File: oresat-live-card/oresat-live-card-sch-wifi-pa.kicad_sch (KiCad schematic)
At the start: 29 parts, among them J9 U.FL, U17 PAT1220-C-3DB, U19 TQP9111, U8 MIC94070YC6-TR

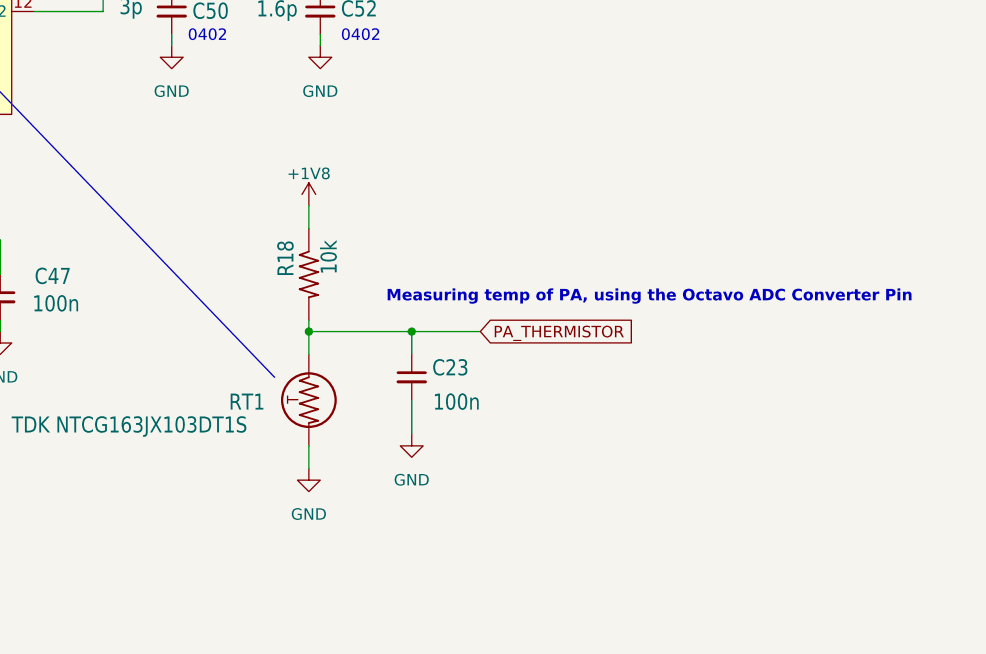
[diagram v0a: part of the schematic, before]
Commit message: Updated SIP A, B, and C. Lots of cleanup of crazy routing - this board is long in the tooth and has been rerouted several times, so there's a lot of crazy routing. Cleaning up a bit is really helping.
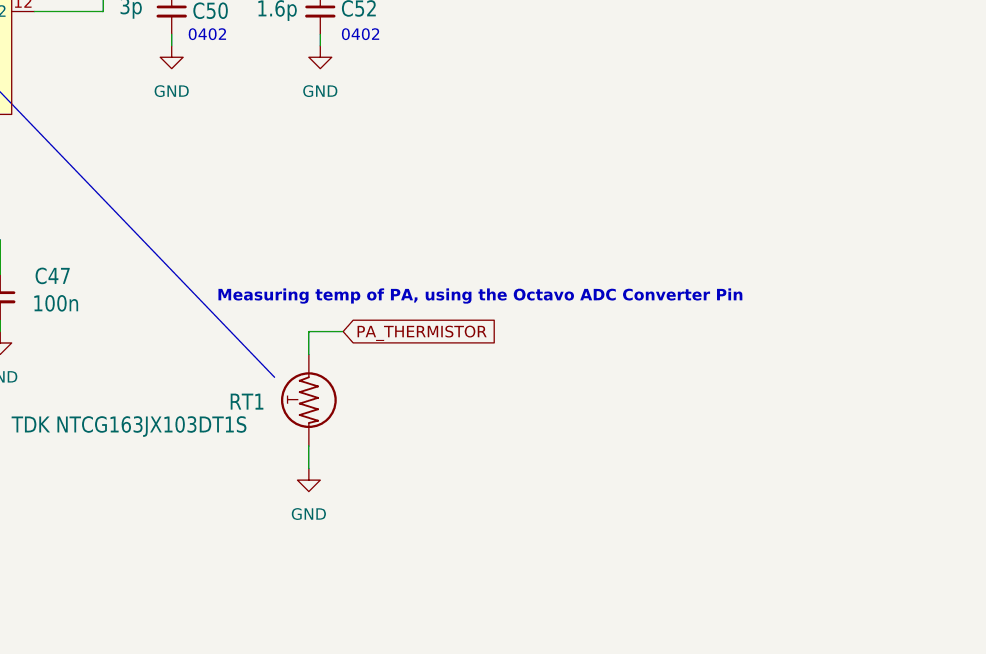
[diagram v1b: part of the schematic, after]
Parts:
- removed C23: 100n, Resistor_SMD:R_0603_1608Metric, symbol Device:C_Small
- removed R18: 10k, Resistor_SMD:R_0603_1608Metric, symbol oresat-passives:R-US

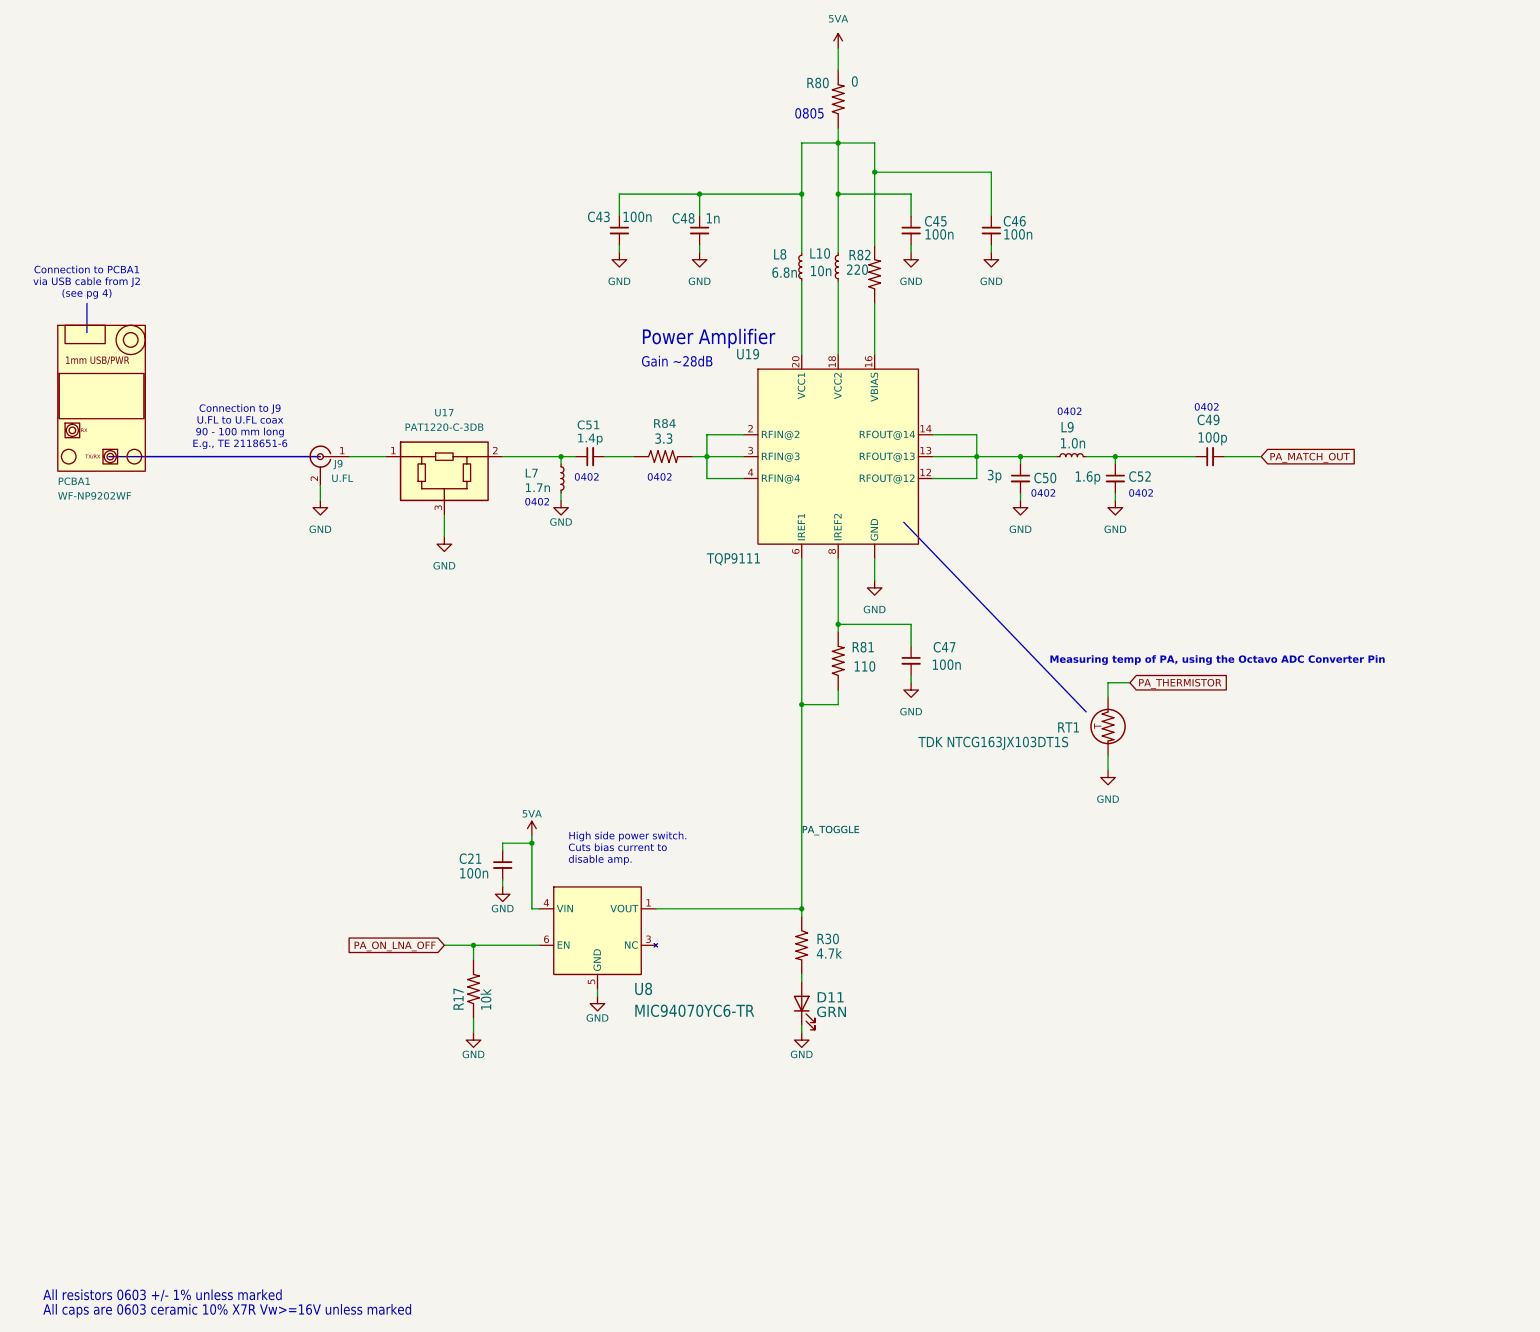
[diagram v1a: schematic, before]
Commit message: Schematic cleaned up and should be good to go. Lots of DRC errors to fix. Also waiting for design review.
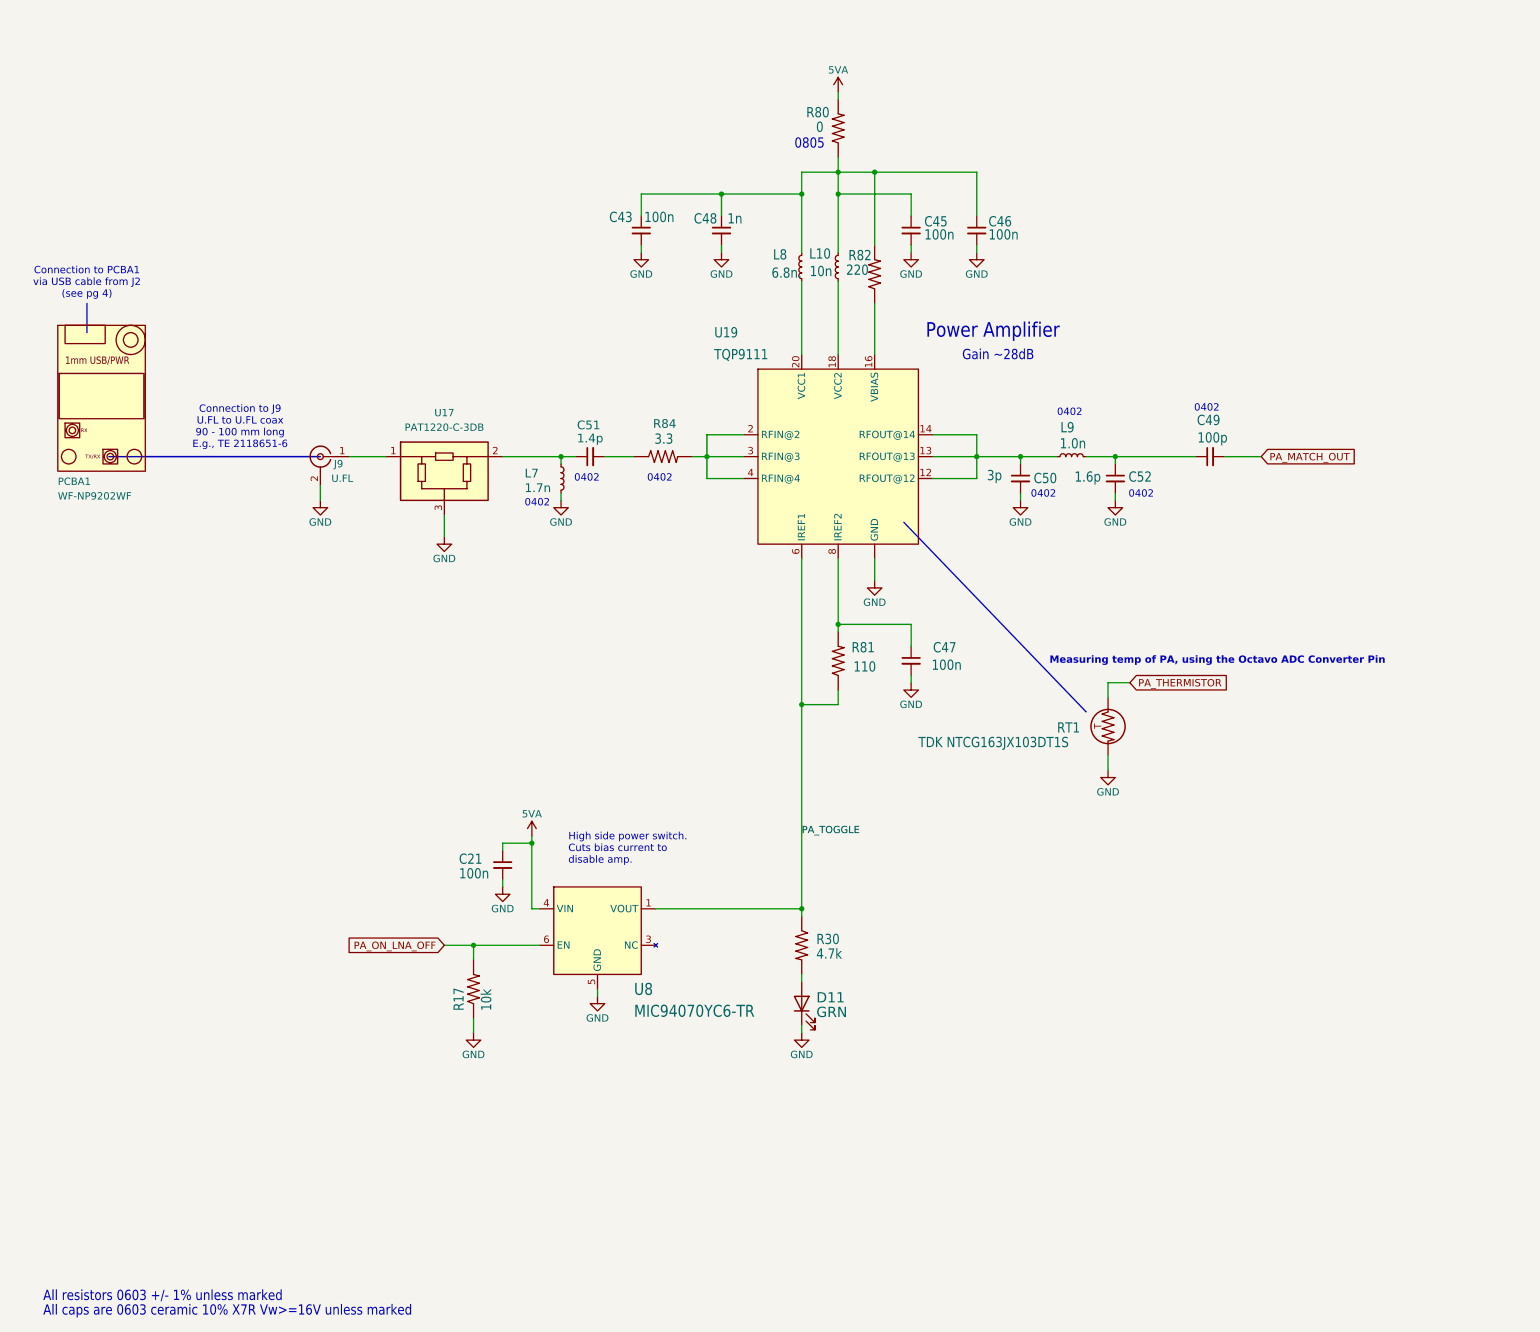
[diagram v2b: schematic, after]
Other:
- moved on the sheet: C43, C46, C48, R80

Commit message: added Olivers BOM and footprint changes, cleaned up pcb
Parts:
- C21, C45, C46, R17, R30, R82: footprint Resistor_SMD:R_0603_1608Metric -> oresat-passives:0603-C
- C43: footprint Resistor_SMD:R_0402_1005Metric -> oresat-passives:0603-C
- C47: footprint Capacitor_SMD:C_0402_1005Metric -> oresat-passives:0603-C
- C48, C49, L9, R81, R84: footprint Resistor_SMD:R_0402_1005Metric -> oresat-passives:0402-C
- C50, C51, C52: footprint Resistor_SMD:R_0402_1005Metric -> oresat-passives:0402-C; DIS (none) -> Mouser
- L10: DIS DigiKey -> Coilcraft
- L7: footprint Resistor_SMD:R_0402_1005Metric -> oresat-passives:0402-C; DIS (none) -> DigiKey; DPN 994-0402DC-1N7XJRW -> 2457-0402DC-1N7XJRW-ND; MPN 0402DC-1N7XJRU -> 0402DC-1N7XJRW
- L8: footprint Resistor_SMD:R_0805_2012Metric -> oresat-passives:0805-C; DIS (none) -> DigiKey; DPN 994-0805CS-060XJLC -> 2457-0805CS-060XJRC-ND; MPN 0805CS-060XJLC -> 0805CS-060XJRC
- R80: footprint Resistor_SMD:R_0805_2012Metric -> oresat-passives:0805-C
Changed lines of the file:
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@@
 			)
 		)
-		(property "Footprint" "Resistor_SMD:R_0402_1005Metric"
+		(property "Footprint" "oresat-passives:0402-C"
 			(at 210.82 114.3 0)
 			(effects
@@
 			)
 		)
-		(property "DIS" ""
+		(property "DIS" "Mouser"
 			(at 210.82 114.3 90)
 			(effects
@@
 			)
 		)
-		(property "Footprint" "Resistor_SMD:R_0603_1608Metric"
+		(property "Footprint" "oresat-passives:0603-C"
 			(at 247.65 199.39 0)
 			(effects
@@
 			)
 		)
-		(property "Footprint" "Resistor_SMD:R_0603_1608Metric"
+		(property "Footprint" "oresat-passives:0603-C"
 			(at 266.7 74.93 0)
 			(effects
@@
 			)
 		)
-		(property "Footprint" "Resistor_SMD:R_0402_1005Metric"
+		(property "Footprint" "oresat-passives:0603-C"
 			(at 219.71 74.93 0)
 			(effects
@@
 			)
 		)
-		(property "Footprint" "Resistor_SMD:R_0402_1005Metric"
+		(property "Footprint" "oresat-passives:0402-C"
 			(at 285.75 118.11 0)
 			(effects
@@
 			)
 		)
-		(property "DIS" ""
+		(property "DIS" "Mouser"
 			(at 285.75 118.11 0)
 			(effects
@@
 			)
 		)
-		(property "Footprint" "Capacitor_SMD:C_0402_1005Metric"
+		(property "Footprint" "oresat-passives:0603-C"
 			(at 266.7 149.86 0)
 			(effects
@@
 			)
 		)
-		(property "Footprint" "Resistor_SMD:R_0603_1608Metric"
+		(property "Footprint" "oresat-passives:0603-C"
 			(at 190.5 207.01 0)
 			(effects
@@
 			)
 		)
-		(property "Footprint" "Resistor_SMD:R_0402_1005Metric"
+		(property "Footprint" "oresat-passives:0402-C"
 			(at 233.68 74.93 0)
 			(effects
@@
 			)
 		)
-		(property "Footprint" "Resistor_SMD:R_0402_1005Metric"
+		(property "Footprint" "oresat-passives:0402-C"
 			(at 205.74 118.11 0)
 			(effects
@@
 			)
 		)
-		(property "MPN" "0402DC-1N7XJRU"
+		(property "MPN" "0402DC-1N7XJRW"
 			(at 205.74 118.11 0)
 			(effects
@@
 			)
 		)
-		(property "DPN" "994-0402DC-1N7XJRW"
+		(property "DPN" "2457-0402DC-1N7XJRW-ND"
 			(at 205.74 118.11 0)
 			(effects
@@
 			)
 		)
-		(property "DIS" ""
+		(property "DIS" "DigiKey"
 			(at 205.74 118.11 0)
 			(effects
@@
 			)
 		)
-		(property "Footprint" "Resistor_SMD:R_0805_2012Metric"
+		(property "Footprint" "oresat-passives:0805-C"
 			(at 247.65 81.28 0)
 			(effects
@@
 			)
 		)
-		(property "Description" "Fixed Inductors 0805CS 6.8 nH 5 % 0.6 A"
+		(property "Description" "FIXED IND 6.8NH 600MA 110MOHM SM"
 			(at 247.65 81.28 0)
 			(effects
@@
 			)
 		)
-		(property "MPN" "0805CS-060XJLC"
+		(property "MPN" "0805CS-060XJRC"
 			(at 247.65 81.28 0)
 			(effects
@@
 			)
 		)
-		(property "DPN" "994-0805CS-060XJLC"
+		(property "DPN" "2457-0805CS-060XJRC-ND"
 			(at 247.65 81.28 0)
 			(effects
@@
 			)
 		)
-		(property "DIS" ""
+		(property "DIS" "DigiKey"
 			(at 247.65 81.28 0)
 			(effects
@@
 			)
 		)
-		(property "Footprint" "Resistor_SMD:R_0603_1608Metric"
+		(property "Footprint" "oresat-passives:0603-C"
 			(at 195.58 185.42 0)
 			(effects
@@
 			)
 		)
-		(property "Footprint" "Resistor_SMD:R_0402_1005Metric"
+		(property "Footprint" "oresat-passives:0402-C"
 			(at 254 149.86 0)
 			(effects
@@
 			)
 		)
-		(property "Footprint" "Resistor_SMD:R_0402_1005Metric"
+		(property "Footprint" "oresat-passives:0402-C"
 			(at 294.64 114.3 0)
 			(effects
@@
 			)
 		)
-		(property "Footprint" "Resistor_SMD:R_0402_1005Metric"
+		(property "Footprint" "oresat-passives:0402-C"
 			(at 302.26 118.11 0)
 			(effects
@@
 			)
 		)
-		(property "DIS" ""
+		(property "DIS" "Mouser"
 			(at 302.26 118.11 0)
 			(effects
@@
 			)
 		)
-		(property "Footprint" "Resistor_SMD:R_0603_1608Metric"
+		(property "Footprint" "oresat-passives:0603-C"
 			(at 278.13 74.93 0)
 			(effects
@@
 			)
 		)
-		(property "Footprint" "Resistor_SMD:R_0805_2012Metric"
+		(property "Footprint" "oresat-passives:0805-C"
 			(at 254 57.15 0)
 			(effects
@@
 			)
 		)
-		(property "DIS" "DigiKey"
+		(property "DIS" "Coilcraft"
 			(at 254 81.28 0)
 			(effects
@@
 			)
 		)
-		(property "Footprint" "Resistor_SMD:R_0402_1005Metric"
+		(property "Footprint" "oresat-passives:0402-C"
 			(at 318.77 114.3 0)
 			(effects
@@
 			)
 		)
-		(property "Footprint" "Resistor_SMD:R_0402_1005Metric"
+		(property "Footprint" "oresat-passives:0402-C"
 			(at 223.52 114.3 0)
 			(effects
@@
 			)
 		)
-		(property "Footprint" "Resistor_SMD:R_0603_1608Metric"
+		(property "Footprint" "oresat-passives:0603-C"
 			(at 260.35 82.55 0)
 			(effects

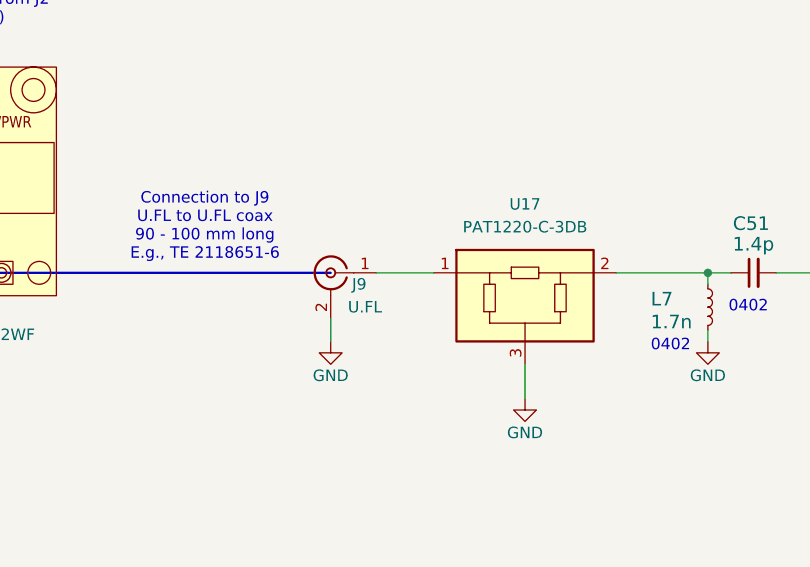
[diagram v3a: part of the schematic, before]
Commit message: Added solder mask to RF traces and assigned RF net classes between U28 pin 6 and U29 pin 2
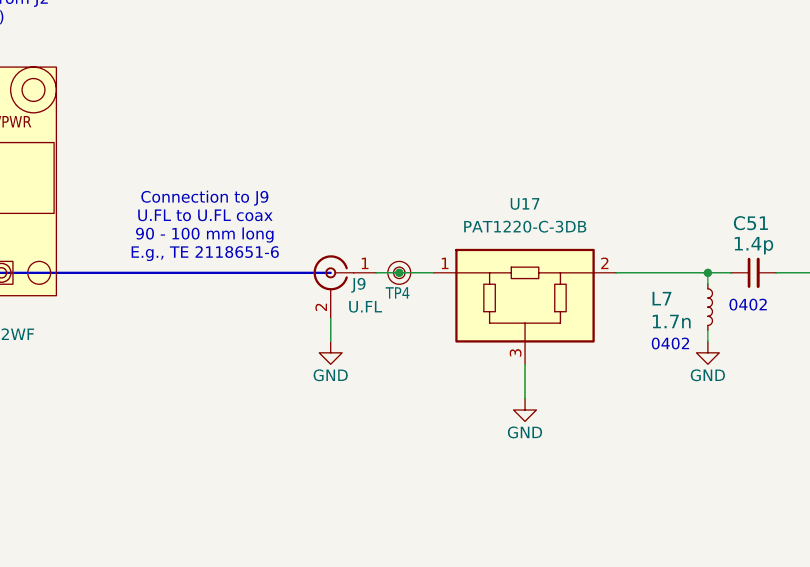
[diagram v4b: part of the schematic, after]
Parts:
- added TP4: ~, oresat-misc:TestPoint_RF_Probe, symbol oresat-misc:Test-Point-RF-Probe-Stripline
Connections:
- net at J9.1 (In), U17.1: now also TP4.1
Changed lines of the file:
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@@
 	)
 	(junction
+		(at 171.45 114.3)
+		(diameter 0)
+		(color 0 0 0 0)
+	)
+	(junction
 		(at 254 143.51)
 		(diameter 0)
@@
 	(wire
 		(pts
+			(xy 171.45 114.3) (xy 175.26 114.3)
+		)
+		(stroke
+			(width 0)
+			(type default)
+		)
+	)
+	(wire
+		(pts
 			(xy 254 154.94) (xy 254 157.48)
 		)
@@
 	(wire
 		(pts
-			(xy 168.91 114.3) (xy 175.26 114.3)
+			(xy 168.91 114.3) (xy 171.45 114.3)
 		)
 		(stroke
@@
 					(unit 1)
 				)
+			)
+		)
+	)
+	(symbol
+		(lib_id "oresat-misc:Test-Point-RF-Probe-Stripline")
+		(at 171.45 114.3 90)
+		(unit 1)
+		(exclude_from_sim no)
+		(in_bom no)
+		(on_board yes)
+		(dnp no)
+		(property "Reference" "TP4"
+			(at 169.926 116.586 90)
+			(effects
+				(font
+					(size 1.27 1.0795)
+				)
+				(justify right)
+			)
+		)
+		(property "Value" "~"
+			(at 163.83 114.3 0)
+			(effects
+				(font
+					(size 1.27 1.27)
+				)
+				(hide yes)
+			)
+		)
+		(property "Footprint" "oresat-misc:TestPoint_RF_Probe"
+			(at 161.29 114.3 0)
+			(effects
+				(font
+					(size 1.27 1.27)
+				)
+				(hide yes)
+			)
+		)
+		(property "Datasheet" ""
+			(at 171.45 114.3 0)
+			(effects
+				(font
+					(size 1.27 1.27)
+				)
+				(hide yes)
+			)
+		)
+		(property "Description" "Special test point symbol for RF3B-BC2.0 3 needle RFspring probe"
+			(at 164.084 114.046 0)
+			(effects
+				(font
+					(size 1.27 1.27)
+				)
+				(hide yes)
+			)
+		)
+		(pin "1"
+		)
+		(instances
+			(project ""
+				(path "/748bdd2d-da0a-4240-ba60-0bf881d2ec56/05da2a2f-8aac-4f69-92b0-4622cd97ee54"
+					(reference "TP4")
+					(unit 1)
+				)

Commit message: added 100p cap to U34 CTRL line, some BOM changes
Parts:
- R30: DPN ERJ-3EKF4701V -> P4.70KHCT-ND
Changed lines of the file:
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@@
 			)
 		)
-		(property "DPN" "ERJ-3EKF4701V"
+		(property "DPN" "P4.70KHCT-ND"
 			(at 247.65 199.39 0)
 			(effects

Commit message: Components Update
Changed Debug connector and performed minor rerouting
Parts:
- TP4: value ~ -> (none)
